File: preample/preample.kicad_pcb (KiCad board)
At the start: 2 copper layers, 27 parts, among them SW1 SW_DPDT_x2, U1 TPS7A39, U2 OPA2134UA, U3 OPA134UA, U4 OPA2134UA, U5 OPA134UA

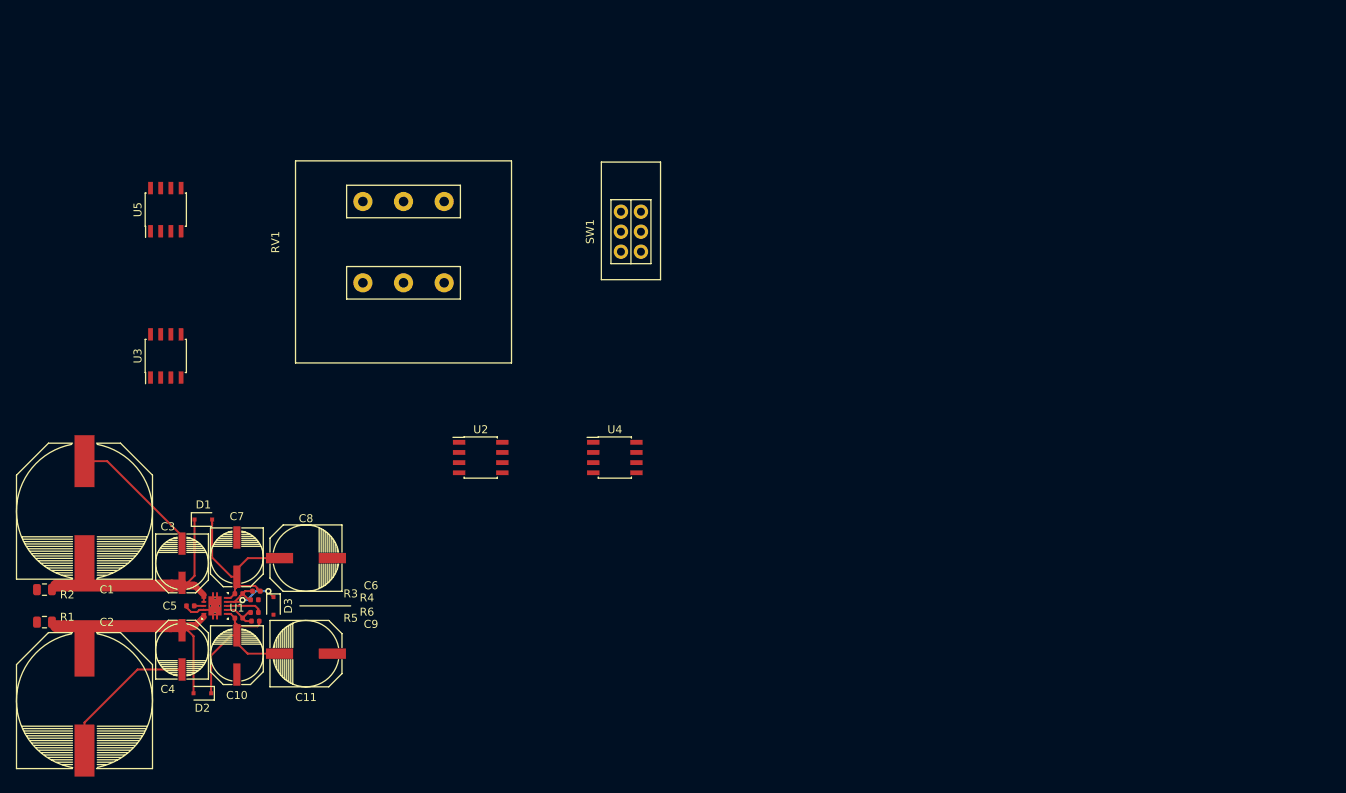
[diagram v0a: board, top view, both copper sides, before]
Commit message: swapped 10uF psu caps for smaller ceramics. assigned footprints to many passives. more pcb layout.
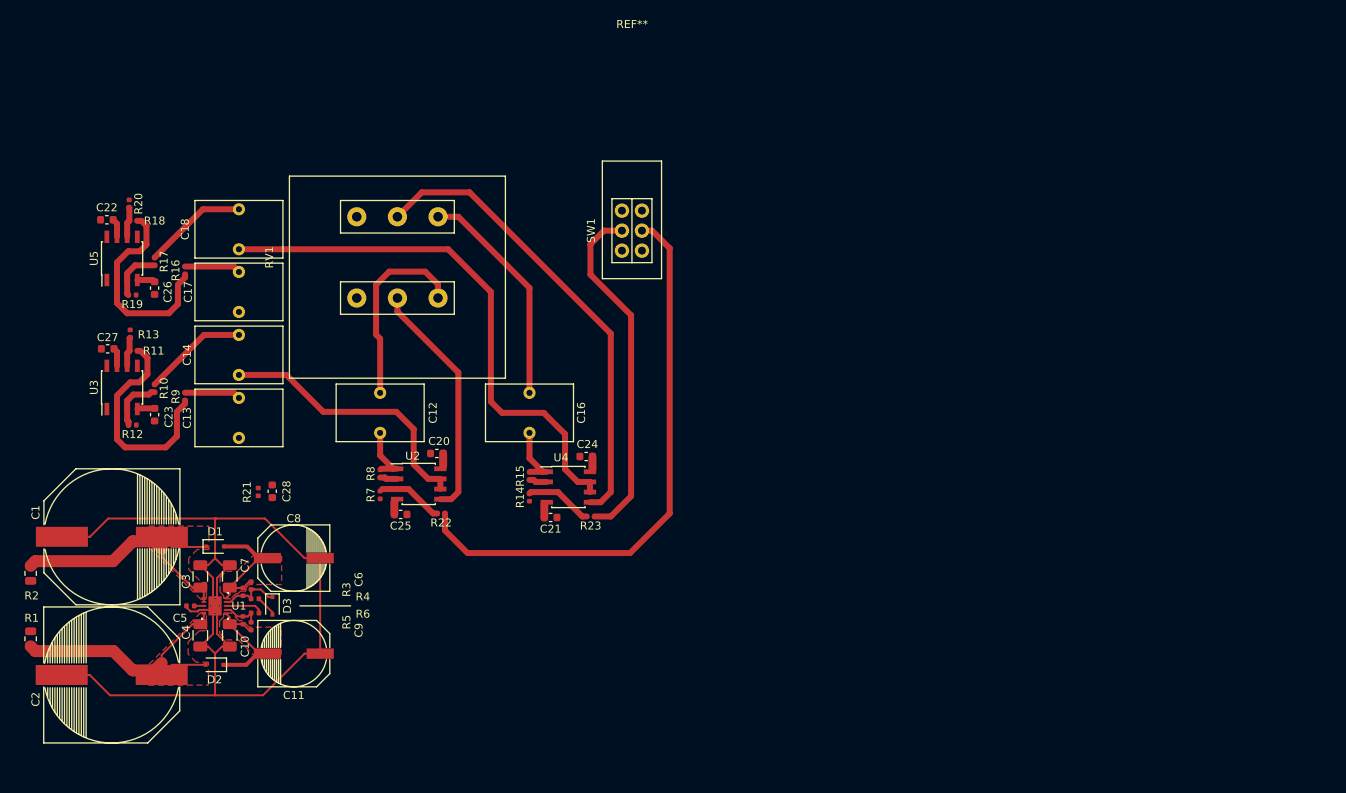
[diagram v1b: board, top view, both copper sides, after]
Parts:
- added C12: 10uF, preample:MKS2B051001N00JSSD, F.Cu at (85.5, 90.2)
- added C13: 10uF, preample:MKS2B051001N00JSSD, F.Cu at (67.8, 90.8)
- added C14: 10uF, preample:MKS2B051001N00JSSD, F.Cu at (67.8, 82.9)
- added C16: 10uF, preample:MKS2B051001N00JSSD, F.Cu at (104.1, 90.2)
- added C17: 10uF, preample:MKS2B051001N00JSSD, F.Cu at (67.8, 75.1)
- added C18: 10uF, preample:MKS2B051001N00JSSD, F.Cu at (67.8, 67.2)
- added C20: 100nF, Capacitor_SMD:C_0603_1608Metric, F.Cu at (92.6, 95.2)
- added C21: 100nF, Capacitor_SMD:C_0603_1608Metric, F.Cu at (106.8, 103.3)
- added C22: 100nF, Capacitor_SMD:C_0603_1608Metric, F.Cu at (51.3, 66.0)
- added C23: 100nF, Capacitor_SMD:C_0603_1608Metric, F.Cu at (57.3, 90.4)
- added C24: 100nF, Capacitor_SMD:C_0603_1608Metric, F.Cu at (111.2, 95.6)
- added C25: 100nF, Capacitor_SMD:C_0603_1608Metric, F.Cu at (88.0, 102.9)
- added C26: 100nF, Capacitor_SMD:C_0603_1608Metric, F.Cu at (57.3, 74.6)
- added C27: 100nF, Capacitor_SMD:C_0603_1608Metric, F.Cu at (51.4, 82.2)
- added C28: 100nF, Capacitor_SMD:C_0603_1608Metric, F.Cu at (72.0, 100.0)
- added R10: 560R, Resistor_SMD:R_0402_1005Metric, F.Cu at (57.3, 87.1)
- added R11: 560R, Resistor_SMD:R_0402_1005Metric, F.Cu at (54.6, 82.4)
- added R12: 560R, Resistor_SMD:R_0402_1005Metric, F.Cu at (54.5, 91.7)
- added R13: 47R, Resistor_SMD:R_0402_1005Metric, F.Cu at (54.2, 80.3)
- added R14: 47K, Resistor_SMD:R_0402_1005Metric, F.Cu at (104.1, 100.7)
- added R15: 1K, Resistor_SMD:R_0402_1005Metric, F.Cu at (104.1, 98.1)
- added R16: 560R, Resistor_SMD:R_0402_1005Metric, F.Cu at (61.1, 72.4)
- added R17: 560R, Resistor_SMD:R_0402_1005Metric, F.Cu at (57.3, 71.2)
- added R18: 560R, Resistor_SMD:R_0402_1005Metric, F.Cu at (54.6, 66.2)
- added R19: 560R, Resistor_SMD:R_0402_1005Metric, F.Cu at (54.5, 75.4)
- added R20: 47R, Resistor_SMD:R_0402_1005Metric, F.Cu at (54.1, 64.0)
- added R21: 100R, Resistor_SMD:R_0402_1005Metric, F.Cu at (70.2, 100.1)
- added R22: 1K, Resistor_SMD:R_0402_1005Metric, F.Cu at (93.1, 102.7)
- added R23: 1K, Resistor_SMD:R_0402_1005Metric, F.Cu at (111.8, 103.1)
- added R7: 47K, Resistor_SMD:R_0402_1005Metric, F.Cu at (85.5, 100.4)
- added R8: 1K, Resistor_SMD:R_0402_1005Metric, F.Cu at (85.5, 97.8)
- added R9: 560R, Resistor_SMD:R_0402_1005Metric, F.Cu at (61.1, 88.1)
- added REF**: E-Switch_1RBLK, preample:E-Switch_1RBLK, F.Cu at (117.0, 46.8)
- C10, C3, C4, C7: footprint preample:50SVPF10M -> Capacitor_SMD:C_1206_3216Metric
- moved U2 8.42 mm to (90.3, 99.1)
- moved U5 8.18 mm to (53.2, 70.9)
- moved U4 6.88 mm to (109.0, 99.4)
- moved U3 6.73 mm to (53.2, 87.0)
- moved C1 4.69 mm to (51.9, 105.7), turned to 90 degrees
- moved C2 4.67 mm to (51.9, 122.9), turned to 270 degrees
- moved D2 3.87 mm to (64.8, 121.7)
- moved D1 3.67 mm to (64.8, 106.9)
- moved C4 2.92 mm to (63.0, 118.0), turned to 270 degrees
- moved C3 2.82 mm to (63.0, 110.6), turned to 90 degrees
- moved R1 2.71 mm to (41.8, 118.4), turned to 90 degrees
- moved R2 2.67 mm to (41.8, 110.2), turned to 90 degrees
- moved C10 2.60 mm to (66.7, 118.0), turned to 90 degrees
- moved C7 2.57 mm to (66.7, 110.6), turned to 90 degrees
- moved RV1 2.05 mm to (87.6, 70.7)
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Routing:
- net GND: track 42.7 -> 128.9 mm
- net CH1_IN: track 0.00 -> 71.0 mm
- net Net-(C18-Pad2): track 0.00 -> 67.8 mm
- net Net-(RV1-Pad5): track 0.00 -> 58.2 mm
- net CH2_IN: track 0.00 -> 43.9 mm
- net Net-(C14-Pad2): track 0.00 -> 34.4 mm
- net Net-(RV1-Pad2): track 0.00 -> 30.0 mm
- net Net-(C16-Pad1): track 0.00 -> 28.2 mm
- net Net-(R11-Pad2): track 0.00 -> 27.4 mm
- net Net-(R16-Pad1): track 0.00 -> 26.2 mm
- net Net-(C12-Pad1): track 0.00 -> 24.5 mm
- net Net-(C14-Pad1): track 0.00 -> 13.1 mm
- net Net-(C18-Pad1): track 0.00 -> 13.0 mm
- net Net-(R22-Pad2): track 0.00 -> 8.50 mm
- net Net-(R14-Pad2): track 0.00 -> 8.49 mm
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- added copper zone on F.Cu, net +15V
- added copper zone on F.Cu, net +24V
- added copper zone on F.Cu, net -15V
- added copper zone on F.Cu, net -24V

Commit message: all footprints made except connectors. all signal traced laid.
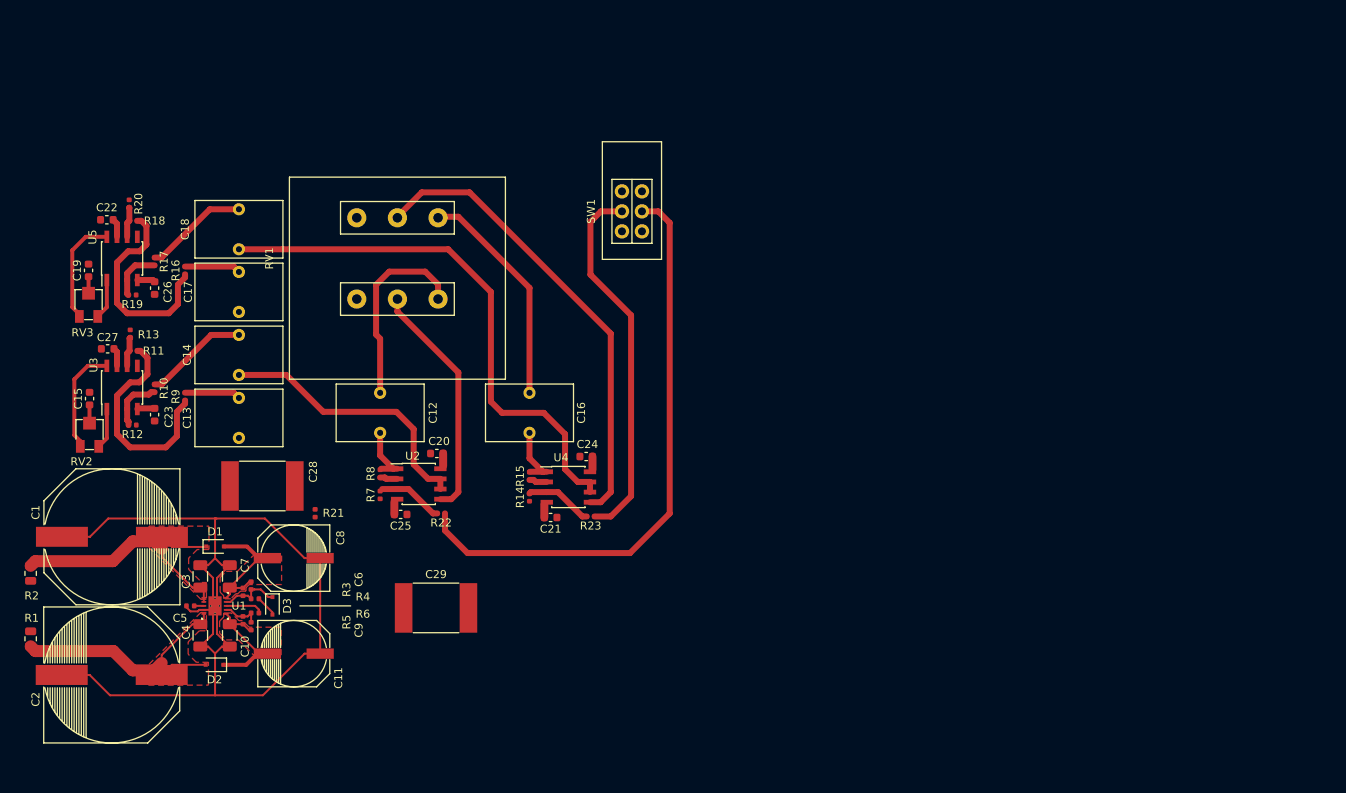
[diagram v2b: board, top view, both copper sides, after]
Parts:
- added C15: 100nF, Capacitor_SMD:C_0603_1608Metric, F.Cu at (49.1, 88.4)
- added C19: 100nF, Capacitor_SMD:C_0603_1608Metric, F.Cu at (49.0, 72.4)
- added C29: 100nF, preample:SMDTD03100TA00KQ00, F.Cu at (92.5, 114.6)
- added REF**: KLN1250B1_4, preample:KLN1250B1_4, F.Cu at (87.6, 40.6)
- added RV2: 100K, preample:22AR100KLFTR, F.Cu at (49.1, 93.7)
- added RV3: 100K, preample:22AR100KLFTR, F.Cu at (49.0, 77.5)
- C28: footprint Capacitor_SMD:C_0603_1608Metric -> preample:SMDTD03100TA00KQ00
- moved R21 7.60 mm to (77.3, 102.7)
- moved SW1 2.41 mm to (116.9, 65.0)
- moved REF** 2.41 mm to (117.0, 44.4)
- moved C28 1.40 mm to (70.8, 99.3), turned to 180 degrees
- moved RV1 0.13 mm to (87.6, 70.9)
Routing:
- net TRIM_2B: track 0.00 -> 13.7 mm
- net TRIM_1B: track 0.00 -> 13.5 mm
- net TRIM_1A: track 0.00 -> 5.09 mm
- net TRIM_2A: track 0.00 -> 5.02 mm
- net CH1_IN: track 71.0 -> 73.8 mm
- net CH2_IN: track 43.9 -> 46.5 mm
- net Net-(C15-Pad1): track 0.00 -> 2.28 mm
- net Net-(C19-Pad1): track 0.00 -> 2.07 mm
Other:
- board text added: "FRONT FACEPLATE"

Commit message: reorganized PCB to fit target chassis
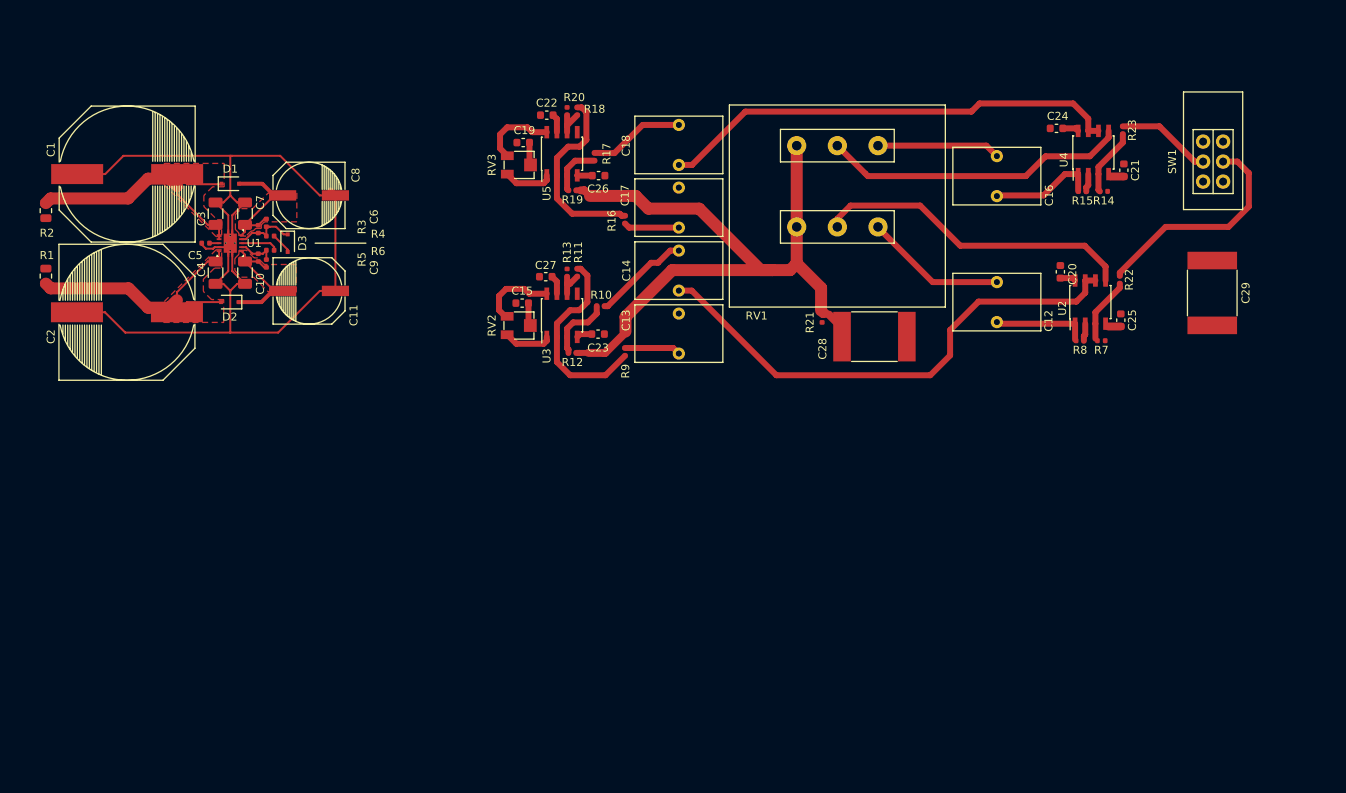
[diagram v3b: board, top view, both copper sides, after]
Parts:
- moved C29 104.7 mm to (189.5, 75.2), turned to 270 degrees
- moved C25 93.2 mm to (178.1, 78.6), turned to 270 degrees
- moved R7 92.2 mm to (175.6, 81.2), turned to 180 degrees
- moved R22 89.7 mm to (177.9, 73.5), turned to 270 degrees
- moved R8 89.0 mm to (173.0, 81.2), turned to 180 degrees
- moved U2 87.0 mm to (174.2, 76.3), turned to 90 degrees
- moved C21 83.8 mm to (178.4, 59.8), turned to 270 degrees
- moved R23 82.2 mm to (178.3, 54.8), turned to 270 degrees
- moved R14 81.3 mm to (175.9, 62.5), turned to 180 degrees
- moved C20 81.2 mm to (170.5, 72.5), turned to 270 degrees
- moved C28 78.7 mm to (147.3, 80.6), turned to 0 degrees
- moved C12 78.3 mm to (162.6, 76.3)
- moved U4 77.8 mm to (174.6, 57.6), turned to 90 degrees
- moved R15 77.7 mm to (173.3, 62.5), turned to 180 degrees
- moved SW1 72.9 mm to (189.6, 58.8)
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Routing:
- net SIGNAL_GROUND: track 0.00 -> 90.5 mm
- net CH1_IN: track 73.8 -> 27.9 mm
- net CH2_IN: track 46.5 -> 11.9 mm
- net Net-(C14-Pad2): track 34.4 -> 64.1 mm
- net Net-(RV1-Pad5): track 58.2 -> 38.3 mm
- net Net-(C16-Pad1): track 28.2 -> 15.4 mm
- net Net-(RV1-Pad2): track 30.0 -> 40.1 mm
- net Net-(C18-Pad2): track 67.8 -> 57.9 mm
- net Net-(C12-Pad1): track 24.5 -> 17.8 mm
- net Net-(C16-Pad2): track 8.22 -> 14.0 mm
- net Net-(C12-Pad2): track 7.82 -> 12.5 mm
- net TRIM_2B: track 13.7 -> 9.50 mm
- net TRIM_1B: track 13.5 -> 9.70 mm
- net Net-(R16-Pad1): track 26.2 -> 24.0 mm
- net Net-(R11-Pad2): track 27.1 -> 24.9 mm
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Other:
- board text added: "3MM FRONT FACEPLATE"
- board text added: "3MM TRAVEL"
- board text removed: "FRONT FACEPLATE"

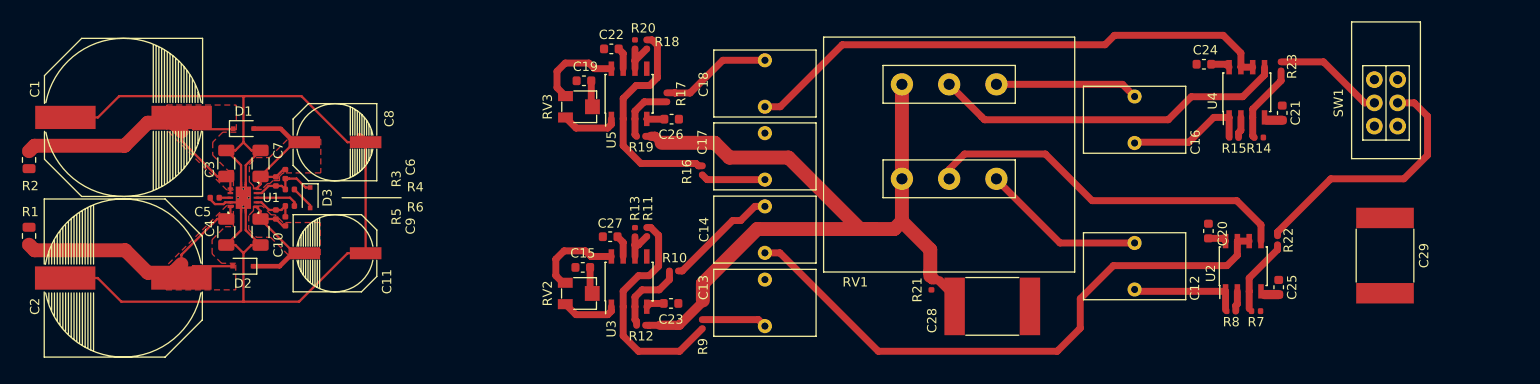
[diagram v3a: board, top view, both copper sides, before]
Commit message: Fixed cap issue in schematic. finished pcb layout
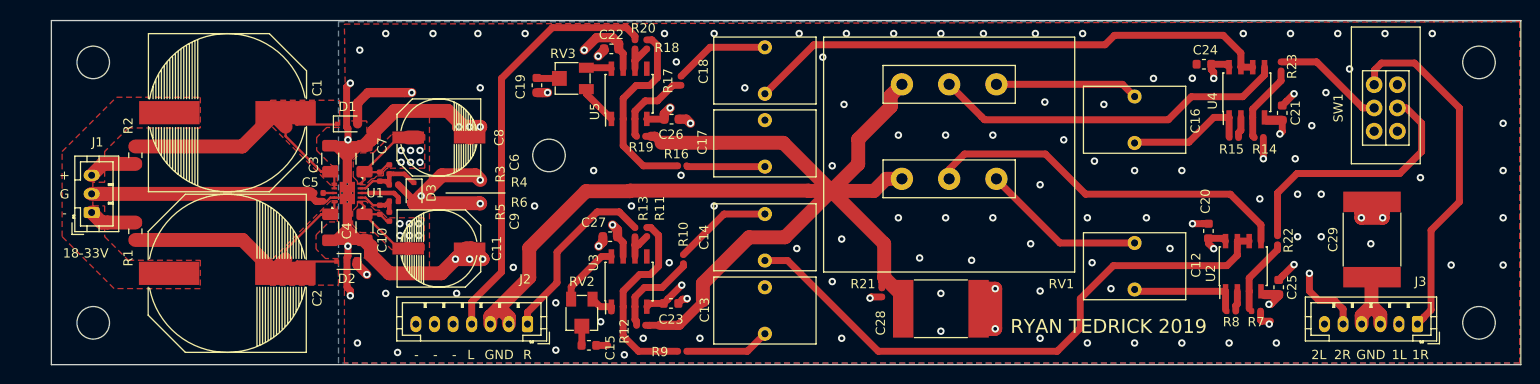
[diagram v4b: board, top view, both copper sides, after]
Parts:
- added J1: Conn_01x03, Connector_JST:JST_PH_B3B-PH-K_1x03_P2.00mm_Vertical, F.Cu at (50.4, 70.5)
- added J2: Conn_01x07, Connector_JST:JST_PH_B7B-PH-K_1x07_P2.00mm_Vertical, F.Cu at (97.3, 82.5)
- added J3: Conn_01x06, Connector_JST:JST_PH_B6B-PH-K_1x06_P2.00mm_Vertical, F.Cu at (193.0, 82.5)
- added REF**: MountingHole_3.5mm, MountingHole:MountingHole_3.5mm, F.Cu at (99.6, 64.4)
- added REF**: MountingHole_3.5mm, MountingHole:MountingHole_3.5mm, F.Cu at (199.6, 54.4)
- added REF**: MountingHole_3.5mm, MountingHole:MountingHole_3.5mm, F.Cu at (199.6, 82.4)
- added REF**: MountingHole_3.5mm, MountingHole:MountingHole_3.5mm, F.Cu at (50.6, 82.4)
- added REF**: MountingHole_3.5mm, MountingHole:MountingHole_3.5mm, F.Cu at (50.6, 54.4)
- moved R1 11.4 mm to (55.1, 72.6)
- moved R2 11.4 mm to (55.1, 64.4)
- moved C1 11.2 mm to (65.0, 59.8), turned to 270 degrees
- moved C10 11.2 mm to (79.8, 72.1)
- moved C11 11.2 mm to (87.8, 74.4)
- moved C2 11.2 mm to (65.0, 77.1), turned to 90 degrees
- moved C6 11.2 mm to (82.4, 65.9)
- moved C7 11.2 mm to (79.8, 64.8)
- moved C8 11.2 mm to (87.8, 62.5)
- moved C9 11.2 mm to (82.4, 71.0)
- moved D1 11.2 mm to (77.9, 61.0)
- moved D2 11.2 mm to (77.9, 75.8)
- moved D3 11.2 mm to (85.1, 68.5)
- moved R3 11.2 mm to (81.4, 66.7)
- moved R4 11.2 mm to (82.9, 67.6)
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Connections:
- C1 pad 1: GND -> +24V
- C1 pad 2: +24V -> GND
- C2 pad 1: -24V -> GND
- C2 pad 2: GND -> -24V
- C4 pad 1: -24V -> GND
- C4 pad 2: GND -> -24V
- RV2 pad 1: TRIM_1A -> TRIM_1B
- RV2 pad 3: TRIM_1B -> TRIM_1A
- RV3 pad 1: TRIM_2A -> TRIM_2B
- RV3 pad 3: TRIM_2B -> TRIM_2A
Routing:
- net -15V: track 25.6 -> 202.8 mm, vias 0 -> 11
- net +15V: track 24.6 -> 182.8 mm, vias 0 -> 11
- net GND: track 129.8 -> 180.6 mm, vias 0 -> 120
- net SIGNAL_GROUND: track 90.5 -> 137.7 mm
- net CH2_OUT: track 0.00 -> 45.1 mm
- net INPUT_B_CH2: track 0.00 -> 38.1 mm
- net INPUT_B_CH1: track 0.00 -> 30.2 mm
- net INPUT_A_CH2: track 0.00 -> 28.8 mm, vias 0 -> 1
- net INPUT_A_CH1: track 0.00 -> 27.0 mm
- net CH1_OUT: track 0.00 -> 19.9 mm
- net INPUT_GND: track 0.00 -> 6.81 mm
- net TRIM_2B: track 9.50 -> 2.73 mm
- net Net-(J1-Pad3): track 0.00 -> 5.20 mm
- net Net-(J1-Pad1): track 0.00 -> 5.15 mm
- net Net-(R11-Pad2): track 24.9 -> 21.2 mm
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- added copper zone on B.Cu, net GND
- added copper zone on F.Cu, net GND
- added copper zone on In1.Cu, net GND
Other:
- board outline added: 158 x 37 mm
- copper layers 2 -> 4
- board text added: "+"
- board text added: "-"
- board text added: "18-33V"
- board text added: "1L"
- board text added: "1R"
- board text added: "2L"
- board text added: "2R"
- board text added: "G"
- board text added: "GND"
- board text added: "L"
- board text added: "R"
- board text added: "RYAN TEDRICK 2019"
